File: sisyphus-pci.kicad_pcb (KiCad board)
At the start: 4 copper layers, 122.3 x 98.7 mm, 124 parts, among them J1 Bus_PCI_32bit_Universal, J10 LINE_OUT, J2 JOYSTICK, J3 CD_IN, J4 WAVE_BLASTER, J5 LINE_IN_HDR, J6 LINE_IN_3.5, J7 HEADPHONE_OUT, J8 PCPCI, J9 LINE_OUT_3.5M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

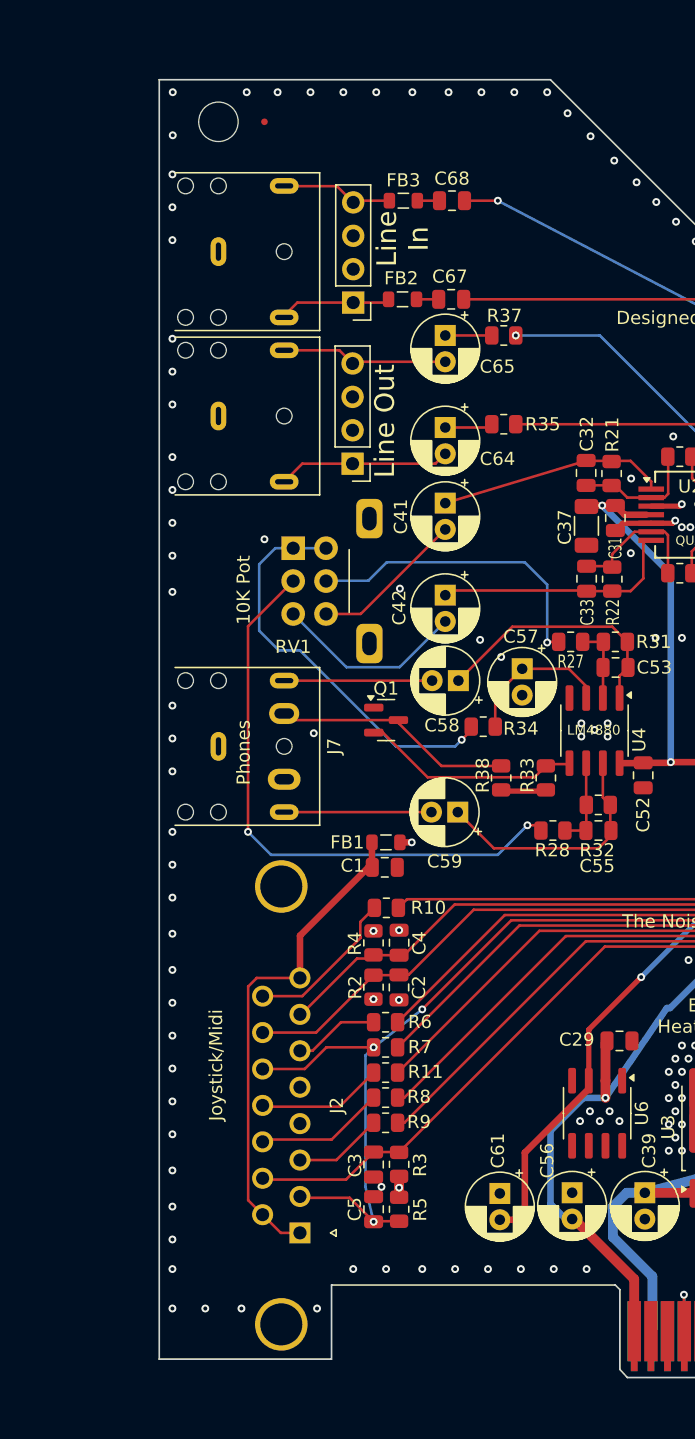
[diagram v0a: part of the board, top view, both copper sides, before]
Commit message: Add files via upload
MAJOR fixes to spacing and what not. Also made a CSV BOM.
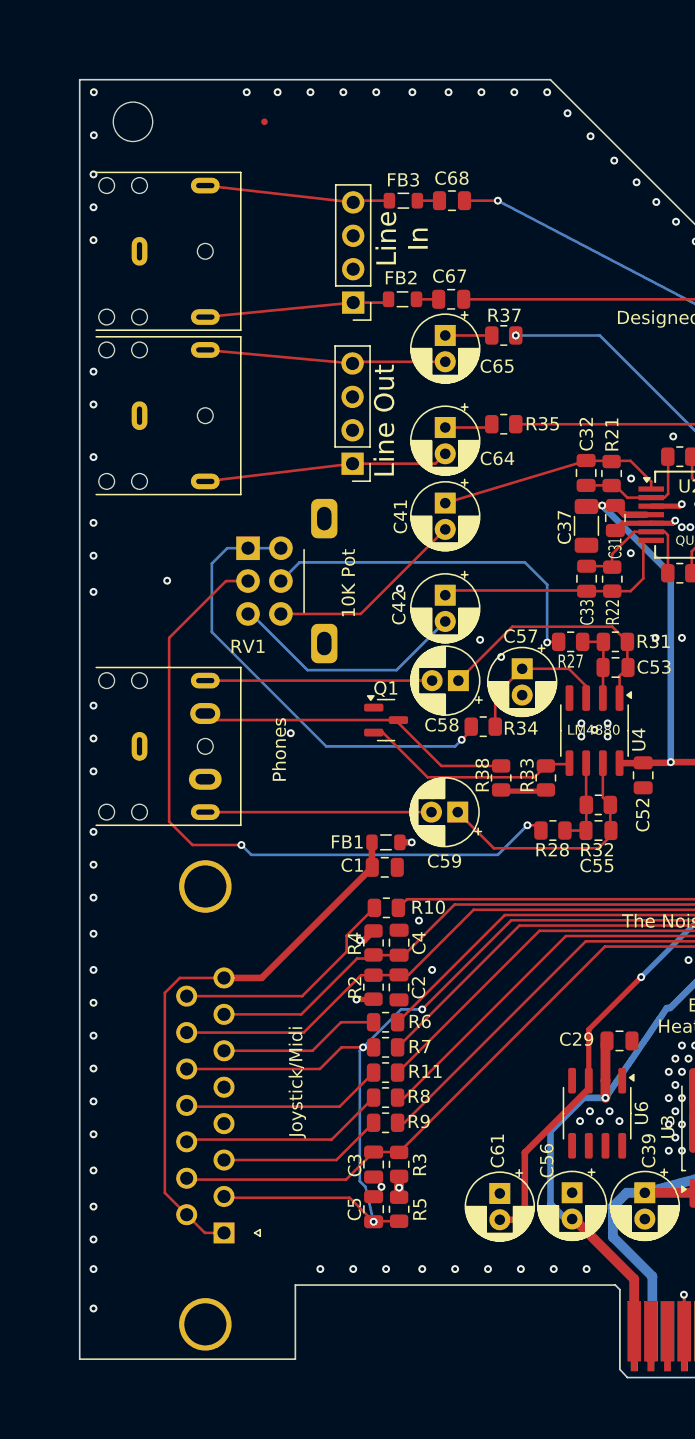
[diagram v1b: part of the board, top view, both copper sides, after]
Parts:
- moved J9 6.00 mm to (43.5, 86.8)
- moved J6 6.00 mm to (43.5, 74.3)
- moved J7 6.00 mm to (43.5, 112.0)
- moved J2 5.78 mm to (49.9, 149.0)
- moved RV1 3.43 mm to (51.8, 96.9)
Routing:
- net Net-(J2-P13): track 102.6 -> 114.6 mm
- net Net-(R28-Pad1): track 44.6 -> 52.2 mm
- net SHUTDOWN: track 17.6 -> 24.3 mm
- net Net-(J2-P111): track 9.59 -> 15.6 mm
- net Net-(J2-P12): track 9.32 -> 15.3 mm
- net Net-(C59-Pad2): track 11.2 -> 17.2 mm
- net Net-(C58-Pad2): track 11.2 -> 17.2 mm
- net Net-(J2-P10): track 87.6 -> 93.5 mm
- net Net-(J10-Pin_4): track 12.7 -> 18.6 mm
- net Net-(U1-SWB): track 76.1 -> 81.9 mm
- net Net-(J2-Pad3): track 6.77 -> 12.5 mm
- net Net-(J2-Pad6): track 6.50 -> 12.3 mm
- net Net-(J2-P14): track 81.6 -> 87.4 mm
- net Net-(J2-P15): track 12.0 -> 17.8 mm
- net Net-(J10-Pin_1): track 13.3 -> 18.9 mm
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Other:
- board size 122.3 x 98.7 mm -> 128.4 x 98.7 mm

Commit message: Add files via upload
Bloody hell... should be okay now.
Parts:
- moved J2 0.56 mm to (50.5, 148.9)
- moved J6 0.55 mm to (44.0, 74.3)
- moved J7 0.55 mm to (44.0, 112.0)
- moved J9 0.55 mm to (44.0, 86.8)
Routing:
- net Net-(U2C--): track 27.0 -> 24.9 mm
- net Net-(J2-P15): track 17.8 -> 16.6 mm
- net Net-(J2-P13): track 114.6 -> 113.5 mm
- net Net-(J2-P9): track 42.6 -> 42.0 mm
- net Net-(J2-P111): track 15.6 -> 15.0 mm
- net SHUTDOWN: track 24.3 -> 23.7 mm
- net Net-(C59-Pad2): track 17.2 -> 16.7 mm
- net Net-(C58-Pad2): track 17.2 -> 16.7 mm
- net Net-(J5-Pin_1): track 14.1 -> 13.5 mm
- net Net-(J5-Pin_4): track 14.1 -> 13.6 mm
- net GND: vias 364 -> 363
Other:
- board size 128.4 x 98.7 mm -> 127.8 x 98.7 mm

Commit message: Add files via upload
Updated to version 0.1a
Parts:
- moved JP1 10.4 mm to (158.5, 89.5)
- moved J8 6.83 mm to (158.5, 138.0)
- moved C15 5.27 mm to (146.2, 133.2)
- moved C14 3.99 mm to (146.2, 129.8)
- moved Y1 3.51 mm to (150.2, 134.0)
- moved FID1 3.27 mm to (162.1, 80.6)
- moved FID4 3.27 mm to (162.1, 147.6)
- moved C11 1.25 mm to (112.5, 129.8)
- moved C40 0.42 mm to (159.2, 150.2)
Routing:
- net MCLK: track 71.2 -> 59.9 mm
- net PCPCIGNTn: track 54.6 -> 46.5 mm
- net PCPCIREQn: track 50.3 -> 42.5 mm
- net SIRQ: track 49.3 -> 41.9 mm
- net Net-(J4-Pin_2): track 4.18 -> 9.04 mm
- net Net-(U1-XI): track 23.2 -> 19.0 mm
- net Net-(U1-XO): track 26.3 -> 22.7 mm
- net /Vcc: track 88.1 -> 91.5 mm
- net /HAD26: track 31.8 -> 31.0 mm
- net CLKRUNn: track 14.0 -> 13.2 mm
- net GND: vias 363 -> 359
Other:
- board size 127.8 x 98.7 mm -> 124.5 x 98.7 mm
- board text added: "Designed by AB V0.1a"
- board text removed: "Designed by AB V0.1"

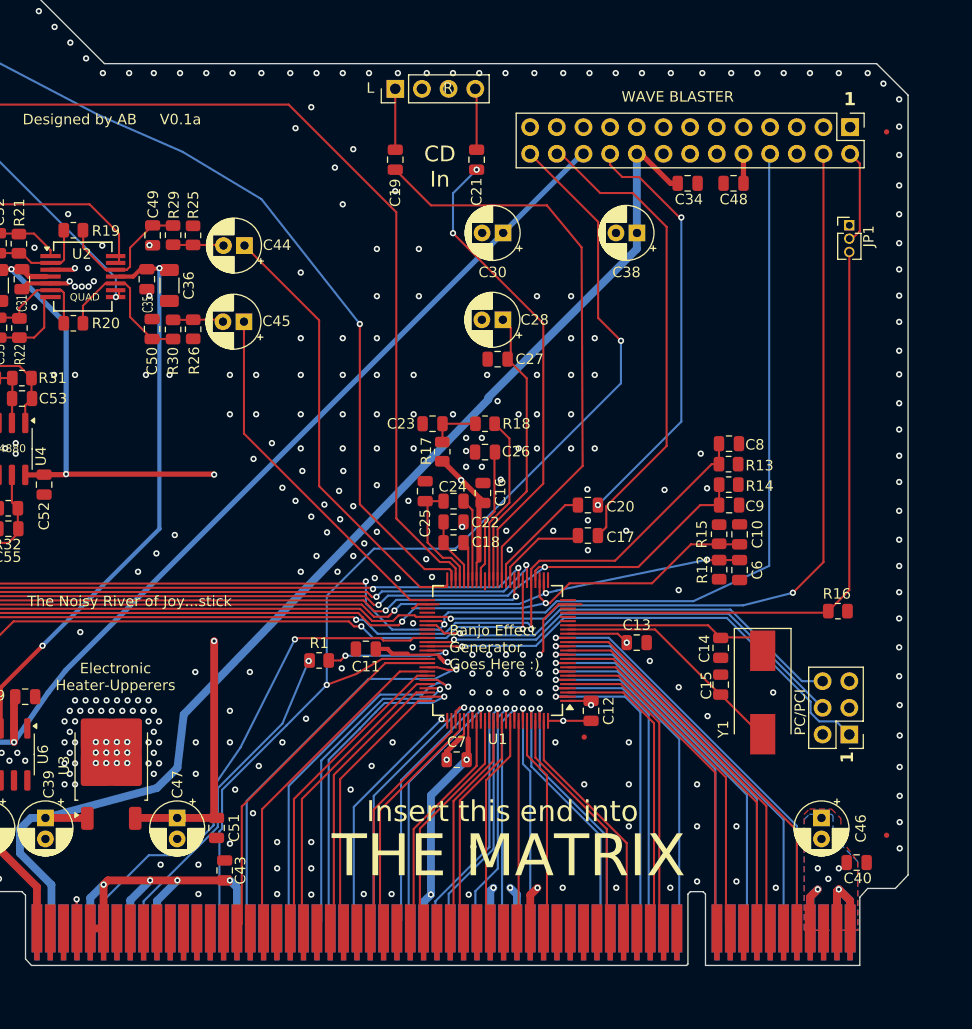
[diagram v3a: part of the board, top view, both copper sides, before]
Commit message: Add files via upload
Smaller board. Smaller and cheaper board means better, right?
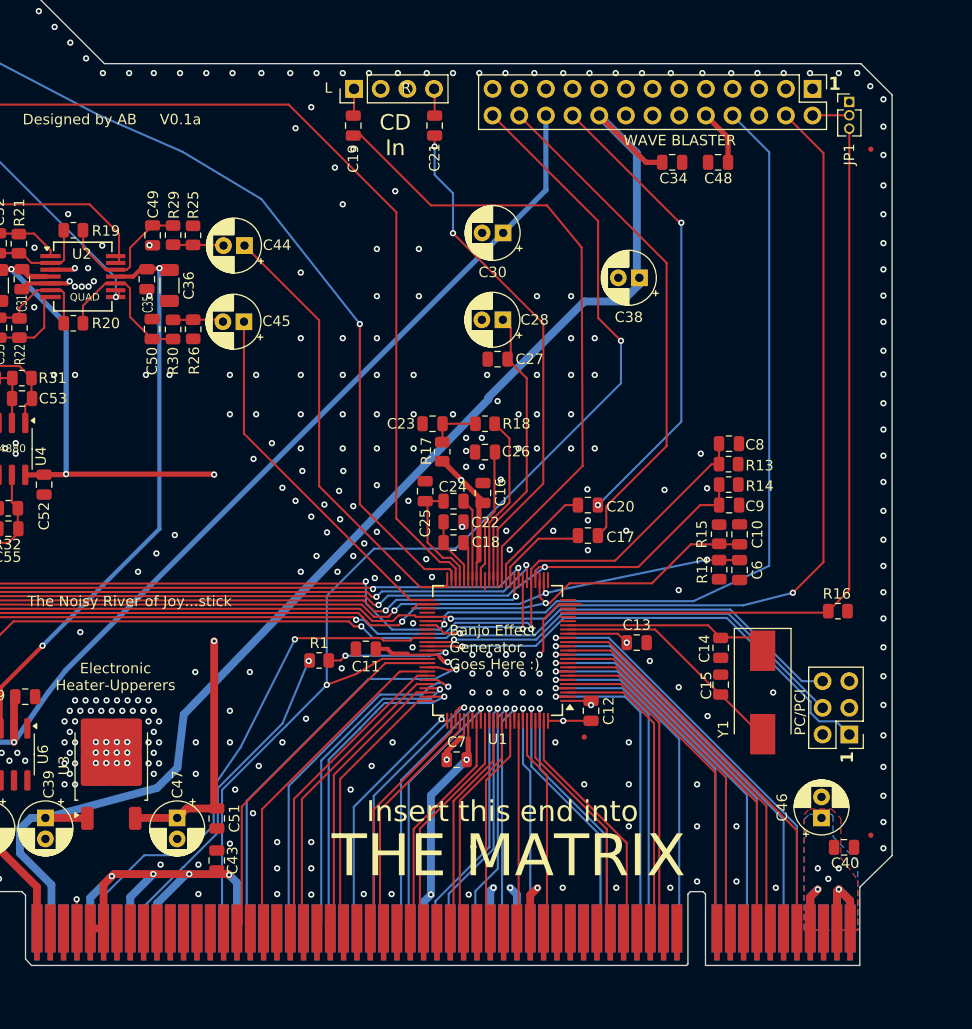
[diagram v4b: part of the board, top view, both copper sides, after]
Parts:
- moved JP1 11.8 mm to (158.5, 77.8)
- moved C19 5.15 mm to (111.2, 80.0)
- moved C21 5.15 mm to (119.0, 80.0)
- moved J4 5.11 mm to (155.0, 76.5)
- moved C38 4.28 mm to (138.5, 94.5)
- moved J3 3.93 mm to (111.3, 76.5)
- moved C34 2.48 mm to (141.6, 83.5)
- moved C48 2.48 mm to (146.0, 83.5)
- moved FID1 2.23 mm to (160.6, 82.2)
- moved C40 1.88 mm to (158.0, 148.8)
- moved FID4 1.50 mm to (160.6, 147.6)
- moved C43 1.21 mm to (98.2, 150.0)
- moved C51 0.90 mm to (98.2, 146.0)
- turned C46 to 90 degrees
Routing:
- net MCLK: track 59.9 -> 71.7 mm
- net /+12V: track 112.3 -> 122.6 mm
- net /Vcc: track 91.5 -> 98.4 mm
- net Net-(J4-Pin_2): track 9.04 -> 3.51 mm
- net Net-(U1-AUXAL): track 55.9 -> 61.3 mm
- net HRSTn: track 110.2 -> 115.3 mm
- net MSOUT: track 139.0 -> 144.1 mm
- net MSIN: track 134.5 -> 139.6 mm
- net WBO_R: track 40.6 -> 44.8 mm
- net Net-(J3-Pin_4): track 5.85 -> 2.57 mm
- net Net-(J3-Pin_1): track 5.80 -> 2.58 mm
- net WBO_L: track 45.5 -> 48.5 mm
- net Net-(U1-AUXAR): track 45.4 -> 48.4 mm
- net /-12V: track 105.2 -> 107.3 mm
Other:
- board size 124.5 x 98.7 mm -> 123 x 98.7 mm

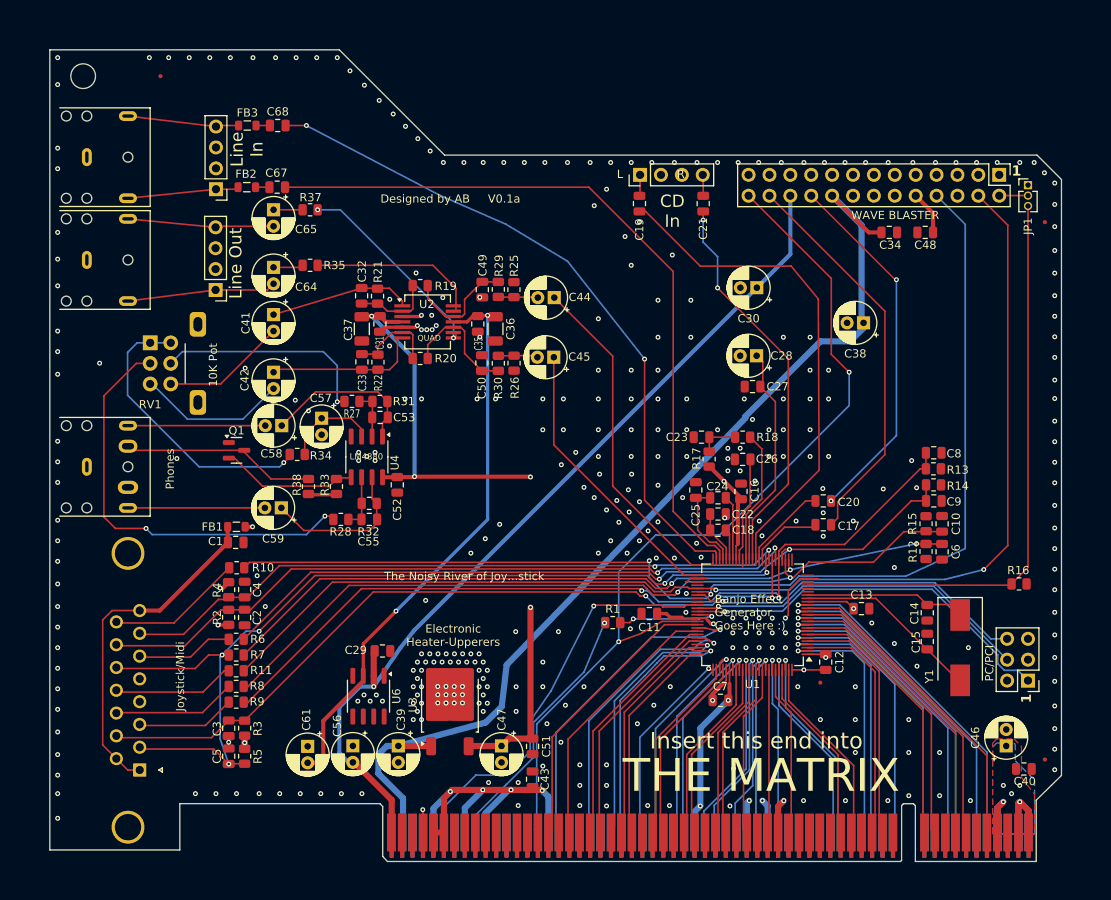
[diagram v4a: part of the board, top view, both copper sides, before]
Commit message: Add files via upload
Introducing the LC branch, which is a cost-reduced version with a much smaller board and reduced jacks etc.
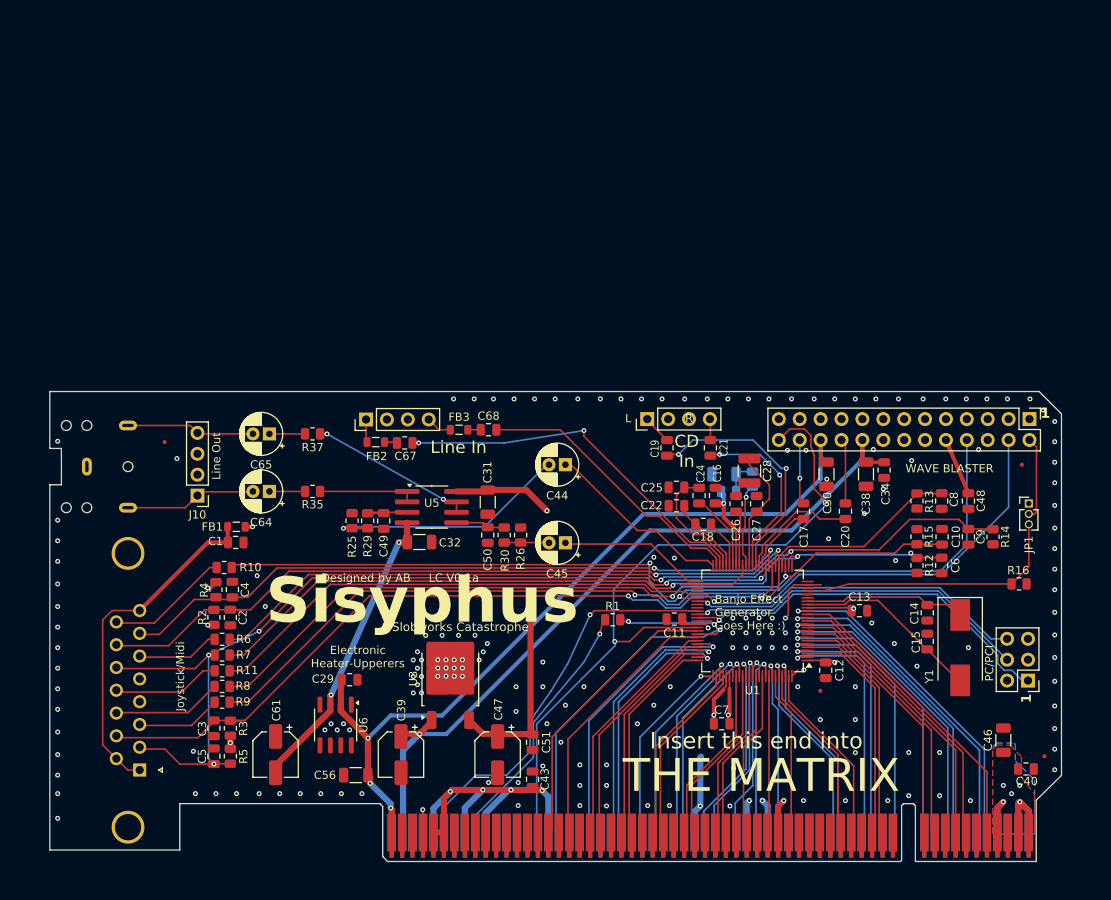
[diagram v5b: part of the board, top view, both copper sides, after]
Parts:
- removed C33: 2200p, Capacitor_SMD:C_0805_2012Metric
- removed C35, C52: 0.1u, Capacitor_SMD:C_0805_2012Metric
- removed C36, C37: 10u, Capacitor_SMD:C_1206_3216Metric
- removed C41, C42: 2.2u_NP, Capacitor_THT:CP_Radial_D5.0mm_P2.00mm
- removed C53, C55: 270p, Capacitor_SMD:C_0805_2012Metric
- removed C57: 1u, Capacitor_THT:CP_Radial_D5.0mm_P2.00mm
- removed C58, C59: 100u_NP, Capacitor_THT:CP_Radial_D5.0mm_P2.00mm
- removed J6: LINE_IN_3.5, Connector_Audio:Jack_3.5mm_CUI_SJ1-3523N_Horizontal
- removed J7: HEADPHONE_OUT, Connector_Audio:Jack_3.5mm_CUI_SJ1-3525N_Horizontal
- removed Q1: BF545A, Package_TO_SOT_SMD:SOT-23
- removed R19, R20: 1.2K, Resistor_SMD:R_0805_2012Metric
- removed R21, R22: 2.7K, Resistor_SMD:R_0805_2012Metric
- removed R27, R28, R31, R32: 20K, Resistor_SMD:R_0805_2012Metric
- removed R33: 100K, Resistor_SMD:R_0805_2012Metric
- removed R34: 50K, Resistor_SMD:R_0805_2012Metric
- removed R38: 1M, Resistor_SMD:R_0805_2012Metric
- removed RV1: 10K, Potentiometer_THT:Potentiometer_Alps_RK09L_Double_Horizontal
- removed U2: BA4564, TSSOP_SSOP:TSSOP_SSOP_14
- removed U4: LM4880, Package_SO:SOIC-8_3.9x4.9mm_P1.27mm
- added G***: LOGO, derp:singin_on_me_banjo, B.Cu at (88.0, 133.7)
- added U5: RC4560, SOIC8_DMP8:SOIC-8_DMP-8, F.Cu at (86.0, 116.9)
- C23: footprint Capacitor_SMD:C_0805_2012Metric -> Capacitor_SMD:C_1206_3216Metric; moved to B.Cu
- C28: footprint Capacitor_THT:CP_Radial_D5.0mm_P2.00mm -> Capacitor_SMD:C_1210_3225Metric
- C30, C38, C46, C56: footprint Capacitor_THT:CP_Radial_D5.0mm_P2.00mm -> Capacitor_SMD:C_1206_3216Metric
- C31: value 0.1u -> 22u; footprint Capacitor_SMD:C_0805_2012Metric -> Capacitor_SMD:C_1206_3216Metric
- C32: value 2200p -> 22u; footprint Capacitor_SMD:C_0805_2012Metric -> Capacitor_SMD:C_1206_3216Metric
- C39, C47, C61: footprint Capacitor_THT:CP_Radial_D5.0mm_P2.00mm -> Capacitor_SMD:CP_Elec_5x5.3
- R17, R18: moved to B.Cu
- moved FB3 45.1 mm to (89.3, 107.5)
- moved C68 45.0 mm to (92.9, 107.5)
- moved FID2 44.5 mm to (53.5, 109.0)
- moved JP1 38.7 mm to (158.6, 116.5)
- moved C67 34.7 mm to (82.7, 109.1)
- moved FB2 34.7 mm to (79.2, 109.0)
- moved R25 34.3 mm to (76.3, 118.6)
- moved J5 33.4 mm to (78.0, 106.2), turned to 90 degrees
- moved C48 33.1 mm to (151.2, 116.2), turned to -90 degrees
- moved R29 32.3 mm to (78.2, 118.6)
- moved C32 30.8 mm to (84.5, 121.2), turned to 0 degrees
- moved C49 30.6 mm to (80.2, 118.6)
- moved J4 29.9 mm to (158.7, 106.2)
- moved C19 29.9 mm to (114.6, 109.7)
- moved C21 29.7 mm to (119.9, 109.7)
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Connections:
- net /AVcc renamed AVcc
- net LO renamed /LO
- net RO renamed /RO
- C32 pad 1: Net-(U2A--) -> AVee
- C32 pad 2: Net-(C32-Pad2) -> GND
- C61 pad 2: /AVee -> AVee
- U6 pad 3: /AVee -> AVee
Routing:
- net /AVee: track 68.5 -> 0.00 mm, vias 2 -> 0
- net Net-(R28-Pad1): track 51.9 -> 0.00 mm, vias 2 -> 0
- net AVcc: track 130.1 -> 81.1 mm, vias 5 -> 3
- net LINE-IN_R: track 82.9 -> 34.2 mm, vias 2 -> 0
- net LINE-IN_L: track 89.4 -> 45.3 mm, vias 0 -> 2
- net WBO_L: track 48.5 -> 7.89 mm, vias 0 -> 1
- net MCLK: track 71.7 -> 33.0 mm
- net WBO_R: track 44.8 -> 7.23 mm, vias 2 -> 0
- net AVee: track 0.00 -> 36.0 mm, vias 0 -> 2
- net /VREF: track 34.8 -> 0.00 mm, vias 1 -> 0
- net Net-(U1-AUXAL): track 61.3 -> 29.9 mm, vias 0 -> 2
- net /+12V: track 122.6 -> 91.4 mm, vias 0 -> 1
- net MSOUT: track 144.1 -> 113.1 mm, vias 2 -> 1
- net MSIN: track 139.6 -> 110.4 mm
- net Net-(R27-Pad1): track 26.8 -> 0.00 mm, vias 1 -> 0
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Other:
- board size 123 x 98.7 mm -> 123 x 57.2 mm
- board text added: "Designed by AB LC V0.1a"
- board text removed: "10K Pot"
- board text removed: "Designed by AB V0.1a"
- board text removed: "LM4880"
- board text removed: "Phones"
- board text removed: "QUAD"
- board text removed: "The Noisy River of Joy...stick"
